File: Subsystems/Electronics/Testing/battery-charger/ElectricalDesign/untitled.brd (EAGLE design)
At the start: 100 x 80 mm, 1 part

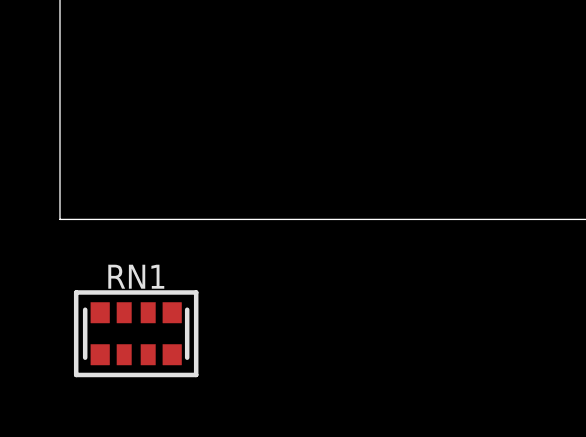
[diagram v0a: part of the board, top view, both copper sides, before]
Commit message: updated schematics
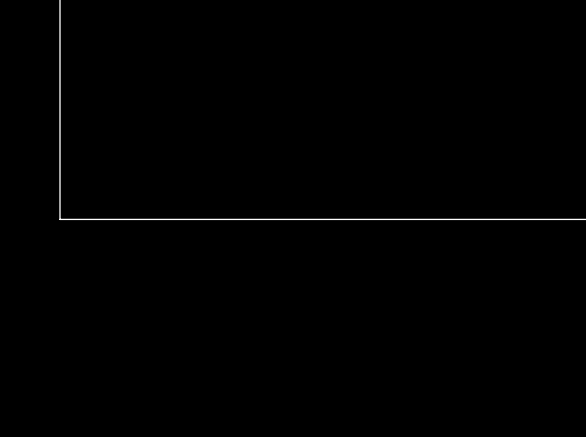
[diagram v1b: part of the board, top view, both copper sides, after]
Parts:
- removed RN1: 10kΩ 1%, CougsInSpace-Resistors:1632
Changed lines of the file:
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@@
 </autorouter>
 <elements>
-<element name="RN1" library="CougsInSpace-Resistors" package="1632" value="10kΩ 1%" x="2.54" y="-3.81" smashed="yes">
-<attribute name="NAME" x="2.54" y="-1.91" size="0.8" layer="25" font="vector" ratio="15" align="center"/>
-<attribute name="PACKAGE" value="1632" x="2.54" y="-3.81" size="1.778" layer="27" display="off"/>
-<attribute name="POWER" value="1/16W" x="2.54" y="-3.81" size="1.778" layer="27" display="off"/>
-<attribute name="SKU" value="26-0000" x="2.54" y="-3.81" size="1.778" layer="27" display="off"/>
-<attribute name="TEMP" value="100ppm/°C" x="2.54" y="-3.81" size="1.778" layer="27" display="off"/>
-</element>
 </elements>
 <signals>
